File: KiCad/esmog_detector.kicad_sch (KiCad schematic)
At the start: 22 parts, among them J10 AudioJack, J9 Conn_Coaxial, Q3 BSR17A, Q4 BC547B, Q5 BC547B, U7 TJM4558CDT

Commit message: changed components and excluded from BOM
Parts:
- D4: JLCPCB Part C7074 -> C12743
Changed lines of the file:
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@@
 			)
 		)
-		(property "JLCPCB Part" "C7074"
+		(property "JLCPCB Part" "C12743"
 			(at 27.94 63.5 0)
 			(hide yes)

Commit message: changed more part#
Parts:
- R25, R27: JLCPCB Part C25804 -> C2930027
- R26, R28: JLCPCB Part C25803 -> C2906980
- R29: JLCPCB Part C21190 -> C2907002
- R30: JLCPCB Part C23193 -> C113299
- R32: JLCPCB Part C4216 -> C844778
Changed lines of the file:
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@@
 			)
 		)
-		(property "JLCPCB Part" "C25803"
+		(property "JLCPCB Part" "C2906980"
 			(at 55.88 77.47 90)
 			(hide yes)
@@
 			)
 		)
-		(property "JLCPCB Part" "C23193"
+		(property "JLCPCB Part" "C113299"
 			(at 114.3 39.37 90)
 			(hide yes)
@@
 			)
 		)
-		(property "JLCPCB Part" "C25804"
+		(property "JLCPCB Part" "C2930027"
 			(at 68.58 35.56 0)
 			(hide yes)
@@
 			)
 		)
-		(property "JLCPCB Part" "C21190"
+		(property "JLCPCB Part" "C2907002"
 			(at 86.36 34.29 0)
 			(hide yes)
@@
 			)
 		)
-		(property "JLCPCB Part" "C25803"
+		(property "JLCPCB Part" "C2906980"
 			(at 83.82 77.47 90)
 			(hide yes)
@@
 			)
 		)
-		(property "JLCPCB Part" "C25804"
+		(property "JLCPCB Part" "C2930027"
 			(at 54.61 35.56 0)
 			(hide yes)
@@
 			)
 		)
-		(property "JLCPCB Part" "C4216"
+		(property "JLCPCB Part" "C844778"
 			(at 151.13 57.15 90)
 			(hide yes)

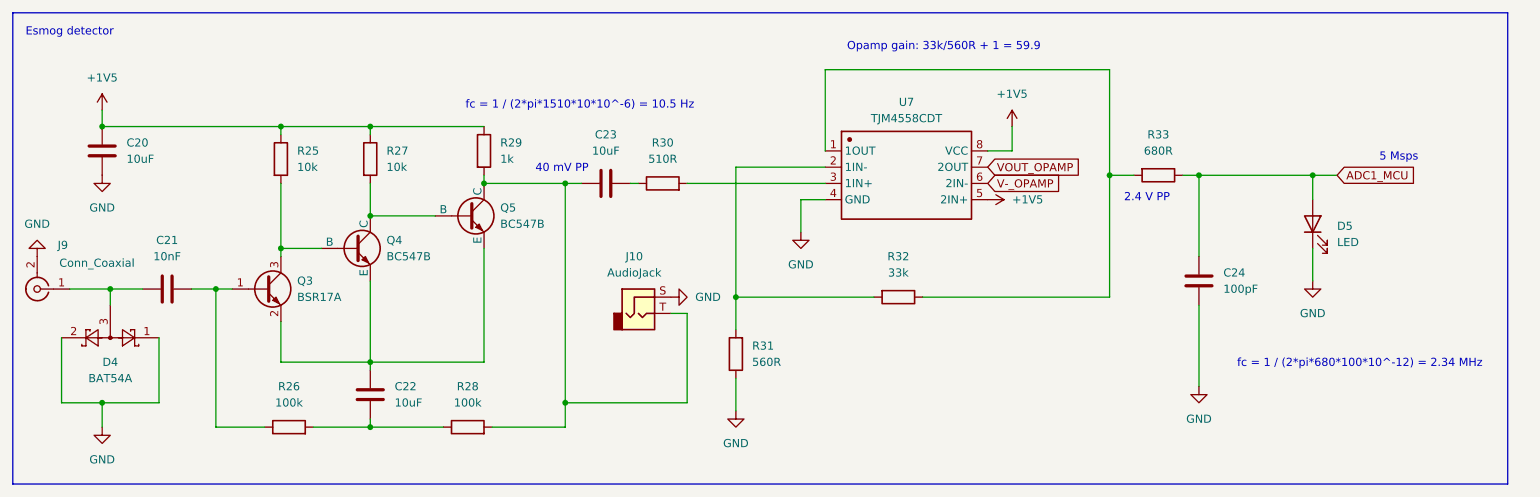
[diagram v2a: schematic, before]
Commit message: changed some out of stock parts
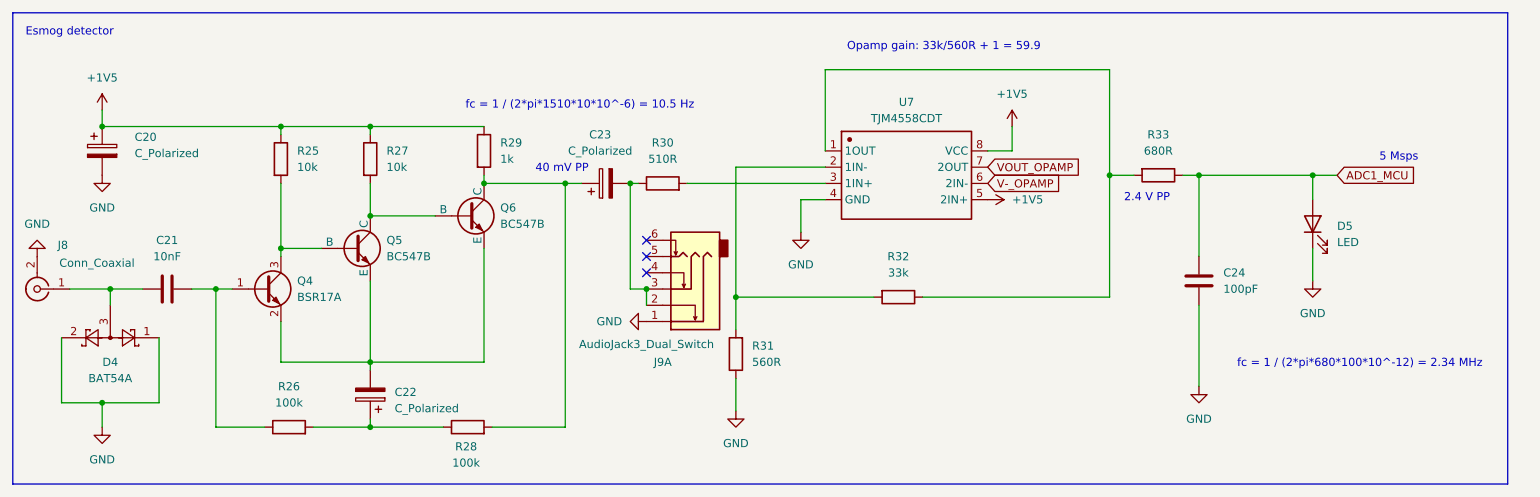
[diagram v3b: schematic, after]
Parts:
- removed C20, C22, C23: 10uF, Capacitor_SMD:C_0603_1608Metric_Pad1.08x0.95mm_HandSolder, symbol Device:C
- removed J10: AudioJack, AV-5:Audio_jack, symbol Connector_Audio:AudioJack2
- added C20, C22, C23: C_Polarized, Capacitor_SMD:CP_Elec_4x5.4, symbol Device:C_Polarized
- added J9: AudioJack3_Dual_Switch, footprints:Audio_jack, symbol Connector_Audio:AudioJack3_Dual_Switch
- J8: renamed from J9; footprint AV-5:CONN-TH_AV-5 -> footprints:CONN-TH_AV-5
- renumbered Q3 to Q4, Q4 to Q5, Q5 to Q6
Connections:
- net +1V5: now also C20.1
- net GND: now also C20.2, J9.1
- net at Q4.2 (E), Q5.3 (E), Q6.3 (E): now also C22.2
- net at R26.2, R28.1: now also C22.1
- net at R30.1: now also C23.2, J9.2, J9.3
- net at Q6.1 (C), R28.2, R29.2: now also C23.1
- no-connect marks 0 -> 3
